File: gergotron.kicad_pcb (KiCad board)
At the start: 2 copper layers, 68.6 x 53.3 mm, 47 parts, among them CON1 ER-OLED-FPC30, J1 KMDGX-6S-BS, J2 KMDGX-6S-BS, J3 AudioJack3_TRS_TN, P1 Power, P2 Analog, P3 Digital, P4 Digital, P5 CONN_01X01, P6 CONN_01X01, P7 CONN_01X01, P8 CONN_01X01, U1 TXB0104D, U2 PCM1808PWG4, U3 CS4334

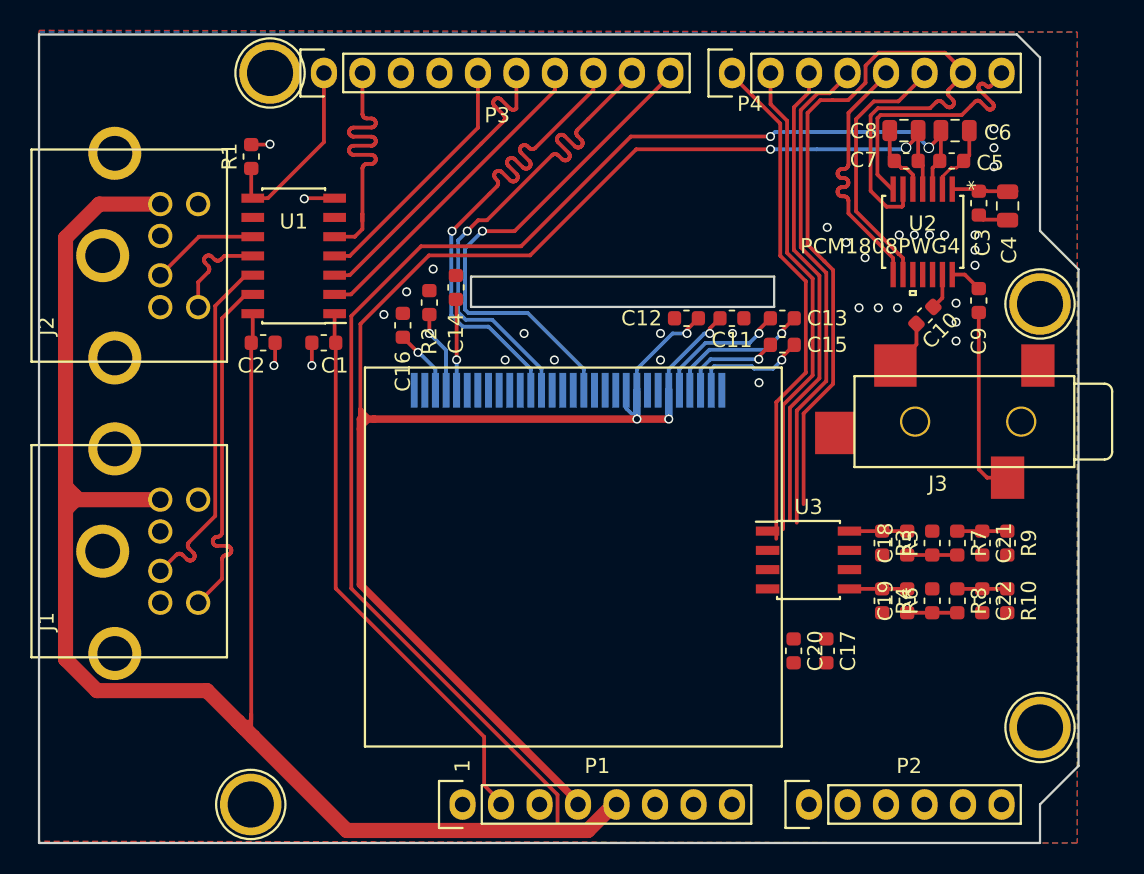
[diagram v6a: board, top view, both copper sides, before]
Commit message: remove audio out
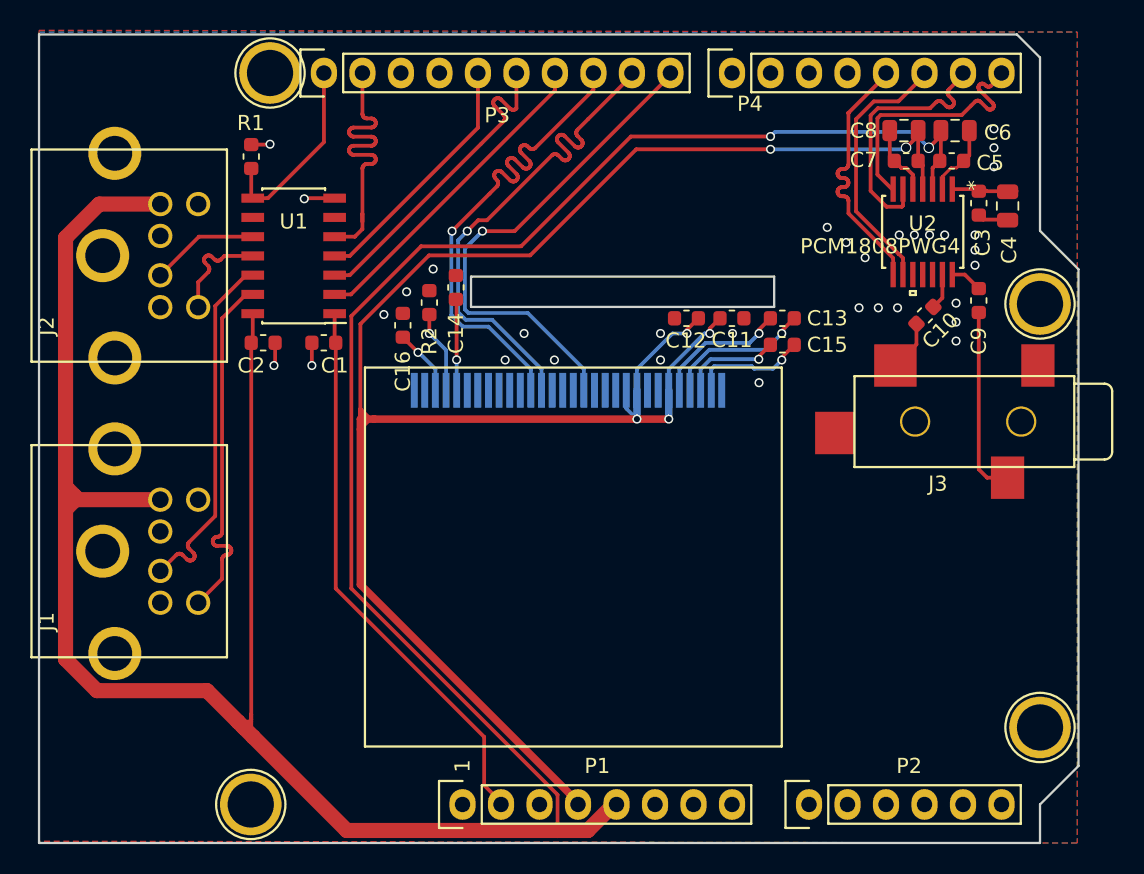
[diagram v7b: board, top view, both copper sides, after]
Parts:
- removed C17: 0.1μF, Capacitor_SMD:C_0603_1608Metric
- removed C18, C19: 3.3μF, Capacitor_SMD:C_0603_1608Metric
- removed C20: 1μF, Capacitor_SMD:C_0603_1608Metric
- removed C21, C22: C, Capacitor_SMD:C_0603_1608Metric
- removed R10, R9: R_Small, Resistor_SMD:R_0603_1608Metric
- removed R3, R4: 267kΩ, Resistor_SMD:R_0603_1608Metric
- removed R5, R6: 10kΩ, Resistor_SMD:R_0603_1608Metric
- removed R7, R8: 560Ω, Resistor_SMD:R_0603_1608Metric
- removed U3: CS4334, Package_SO:SOIC-8_3.9x4.9mm_P1.27mm
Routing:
- net SCKI: track 57.9 -> 17.6 mm
- net Net-(P4-Pad1): track 33.6 -> 0.00 mm
- net DOUT: track 32.9 -> 0.00 mm
- net Net-(P4-Pad2): track 32.1 -> 0.00 mm
- net Net-(P4-Pad3): track 31.4 -> 0.00 mm
- net Net-(C19-Pad2): track 3.81 -> 0.00 mm
- net Net-(C18-Pad2): track 3.81 -> 0.00 mm
- net Net-(C22-Pad1): track 3.30 -> 0.00 mm
- net Net-(C21-Pad1): track 3.30 -> 0.00 mm
- net Net-(C19-Pad1): track 3.30 -> 0.00 mm
- net Net-(C18-Pad1): track 3.30 -> 0.00 mm
